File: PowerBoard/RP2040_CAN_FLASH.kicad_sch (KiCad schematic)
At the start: 52 parts, among them J1 B3B-XH-A_LF__SN_, J2 UJ31-CH-G2-SMT-TR, J4 B3B-XH-A_LF__SN_, J5 Conn_02x10_Counter_Clockwise, Q1 BSS138, Q4 BSS138, Q5 BSS138, Q6 BSS138, U1 RPI2040, U5 W25Q128JVS, U7 MCP2515-xST, U8 MCP2551-I-SN, Y1 445C25D12M00000, Y2 CX532Z-A2B3C5-70-8.0D18

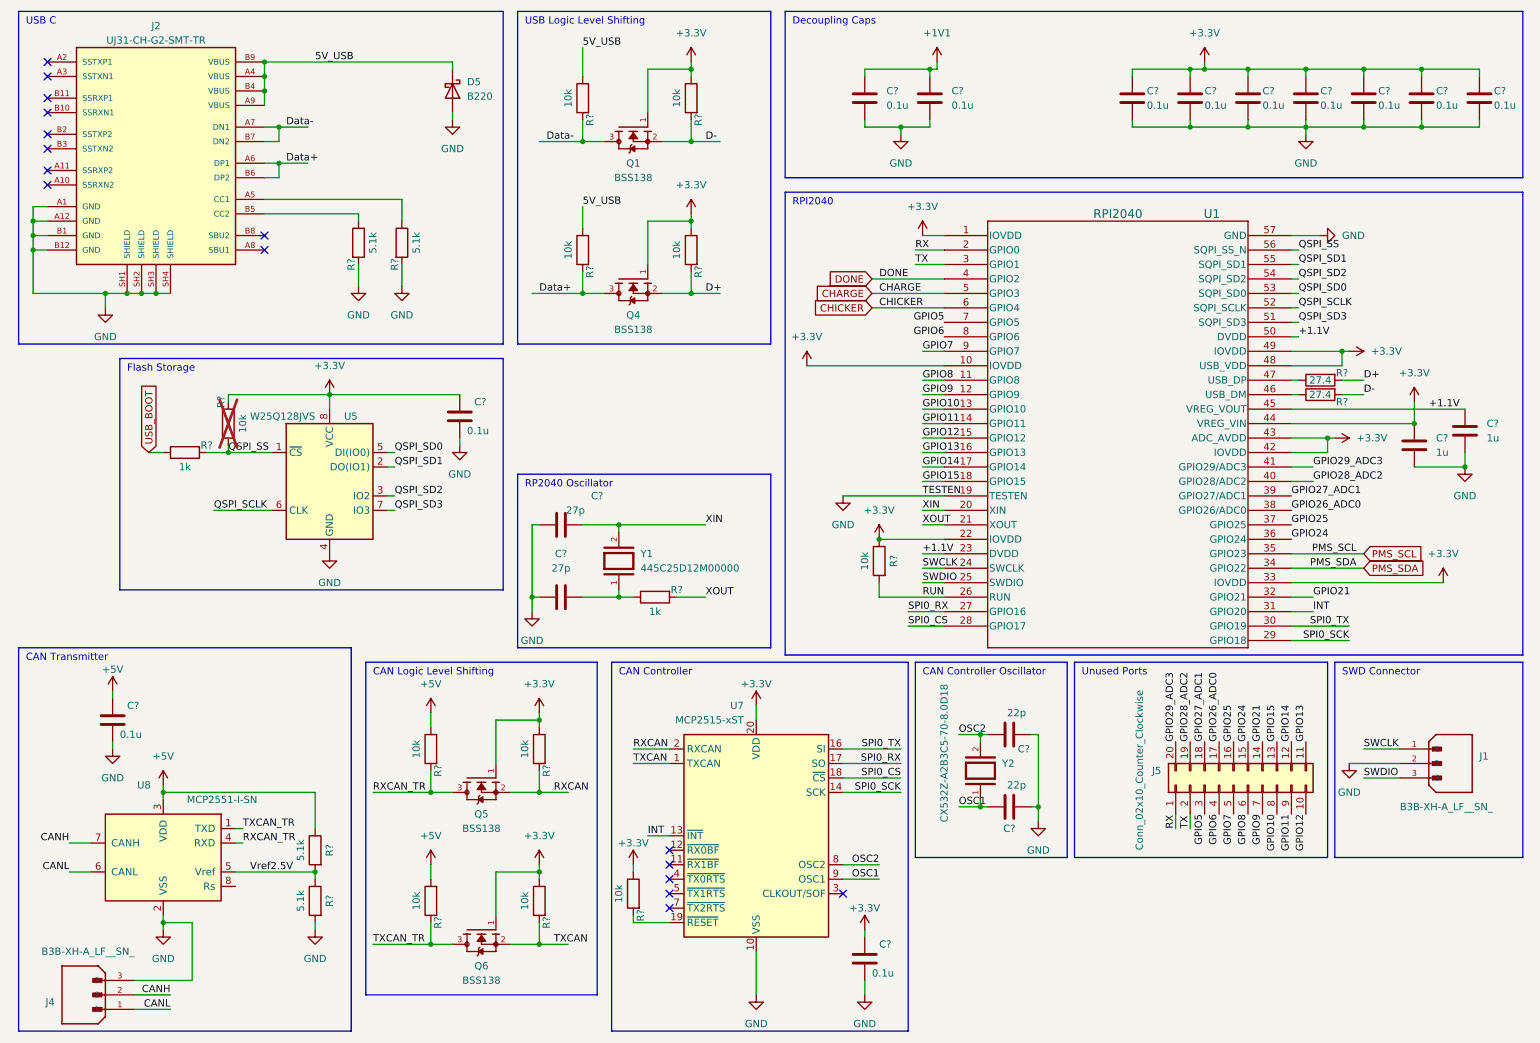
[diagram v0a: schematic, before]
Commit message: updated small details + LEDS
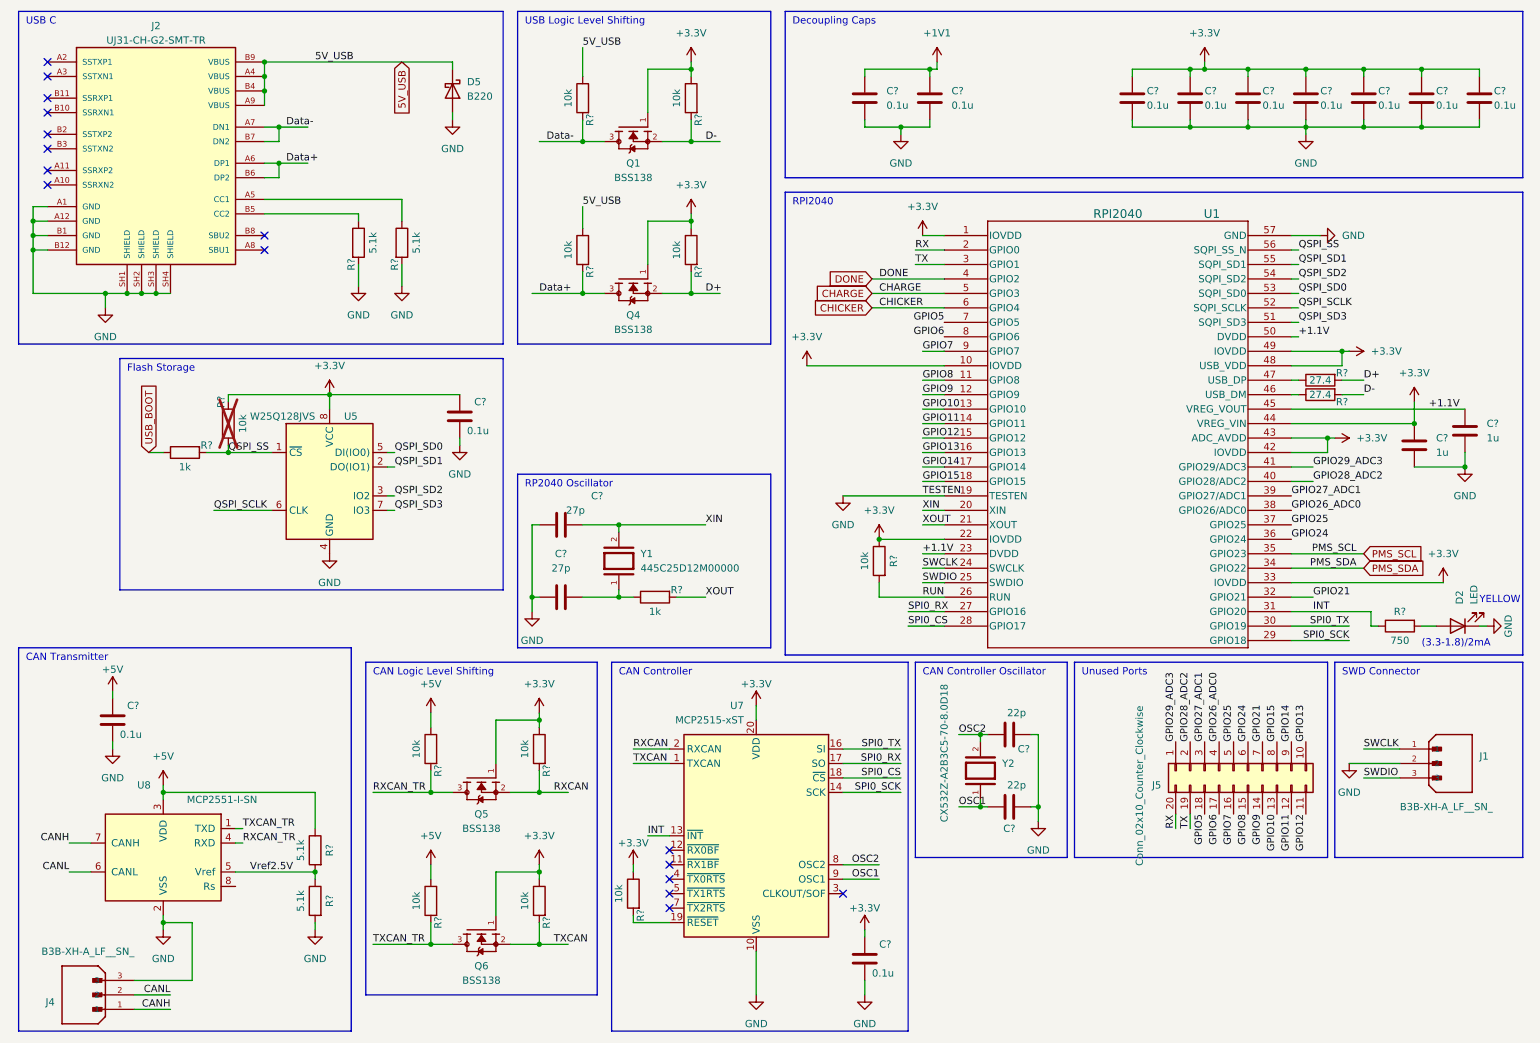
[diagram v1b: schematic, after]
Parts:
- added D2: LED, LED_SMD:LED_1206_3216Metric, symbol Device:LED
- added R?: 750, Resistor_SMD:R_0603_1608Metric, symbol Device:R
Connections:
- net CANH: now also J4.1; no longer J4.2
- net CANL: now also J4.2; no longer J4.1
- net GND: now also D2.1 (K)
- net GPIO10: now also J5.13 (Pin_13); no longer J5.8 (Pin_8)
- net GPIO11: now also J5.12 (Pin_12); no longer J5.9 (Pin_9)
- net GPIO12: now also J5.11 (Pin_11); no longer J5.10 (Pin_10)
- net GPIO13: now also J5.10 (Pin_10); no longer J5.11 (Pin_11)
- net GPIO14: now also J5.9 (Pin_9); no longer J5.12 (Pin_12)
- net GPIO15: now also J5.8 (Pin_8); no longer J5.13 (Pin_13)
- net GPIO21: now also J5.7 (Pin_7); no longer J5.14 (Pin_14)
- net GPIO24: now also J5.6 (Pin_6); no longer J5.15 (Pin_15)
- net GPIO25: now also J5.5 (Pin_5); no longer J5.16 (Pin_16)
- net GPIO26_ADC0: now also J5.4 (Pin_4); no longer J5.17 (Pin_17)
- net GPIO27_ADC1: now also J5.3 (Pin_3); no longer J5.18 (Pin_18)
- net GPIO28_ADC2: now also J5.2 (Pin_2); no longer J5.19 (Pin_19)
- net GPIO29_ADC3: now also J5.1 (Pin_1); no longer J5.20 (Pin_20)
- net GPIO5: now also J5.18 (Pin_18); no longer J5.3 (Pin_3)
- net GPIO6: now also J5.17 (Pin_17); no longer J5.4 (Pin_4)
- net GPIO7: now also J5.16 (Pin_16); no longer J5.5 (Pin_5)
- net GPIO8: now also J5.15 (Pin_15); no longer J5.6 (Pin_6)
- net GPIO9: now also J5.14 (Pin_14); no longer J5.7 (Pin_7)
- net INT: now also R?.1
- net RX: now also J5.20 (Pin_20); no longer J5.1 (Pin_1)
- net TX: now also J5.19 (Pin_19); no longer J5.2 (Pin_2)
- new net: D2.2 (A), R?.2
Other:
- note added: "(3.3-1.8)/2mA"
- note added: "YELLOW"
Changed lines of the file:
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@@
     (stroke (width 0) (type default))
   )
-  (wire (pts (xy 238.76 120.65) (xy 242.57 120.65))
+  (wire (pts (xy 238.76 120.65) (xy 252.73 120.65))
     (stroke (width 0) (type default))
   )
@@
     (stroke (width 0) (type default))
   )
-  (wire (pts (xy 220.98 156.21) (xy 220.98 158.75))
-    (stroke (width 0) (type default))
-  )
   (wire (pts (xy 40.64 152.4) (xy 40.64 151.13))
     (stroke (width 0) (type default))
@@
     (stroke (width 0) (type default))
   )
+  (wire (pts (xy 252.73 123.19) (xy 254 123.19))
+    (stroke (width 0) (type default))
+  )
   (wire (pts (xy 173.99 82.55) (xy 177.8 82.55))
     (stroke (width 0) (type default))
@@
     (stroke (width 0) (type default))
   )
+  (wire (pts (xy 218.44 156.21) (xy 218.44 158.75))
+    (stroke (width 0) (type default))
+  )
   (wire (pts (xy 261.62 35.56) (xy 251.46 35.56))
     (stroke (width 0) (type default))
@@
     (stroke (width 0) (type default))
   )
-  (wire (pts (xy 218.44 156.21) (xy 218.44 158.75))
-    (stroke (width 0) (type default))
-  )
   (wire (pts (xy 24.13 161.29) (xy 27.94 161.29))
     (stroke (width 0) (type default))
@@
     (stroke (width 0) (type default))
   )
+  (wire (pts (xy 271.78 123.19) (xy 273.05 123.19))
+    (stroke (width 0) (type default))
+  )
+  (wire (pts (xy 261.62 123.19) (xy 264.16 123.19))
+    (stroke (width 0) (type default))
+  )
   (wire (pts (xy 69.85 82.55) (xy 69.85 85.09))
     (stroke (width 0) (type default))
@@
     (stroke (width 0) (type default))
   )
+  (wire (pts (xy 252.73 123.19) (xy 252.73 120.65))
+    (stroke (width 0) (type default))
+  )
   (wire (pts (xy 58.42 41.91) (xy 60.96 41.91))
     (stroke (width 0) (type default))
@@
     (stroke (width 0) (type default))
   )
+  (wire (pts (xy 220.98 156.21) (xy 220.98 158.75))
+    (stroke (width 0) (type default))
+  )
   (wire (pts (xy 251.46 144.78) (xy 257.81 144.78))
     (stroke (width 0) (type default))
@@
     (effects (font (size 1.27 1.27)) (justify left bottom))
   )
+  (text "YELLOW" (at 271.78 119.38 0)
+    (effects (font (size 1.27 1.27) (color 251 249 0 1)) (justify left bottom))
+  )
   (text "CAN Controller\n" (at 120.65 132.08 0)
     (effects (font (size 1.27 1.27)) (justify left bottom))
@@
     (effects (font (size 1.27 1.27)) (justify left bottom))
   )
+  (text "(3.3-1.8)/2mA" (at 261.62 127 0)
+    (effects (font (size 1.27 1.27) (color 0 4 0 1)) (justify left bottom))
+  )
   (label "SPI0_CS" (at 171.45 123.19 0) (fields_autoplaced)
     (effects (font (size 1.27 1.27)) (justify left bottom))
@@
     (effects (font (size 1.27 1.27)) (justify left bottom))
   )
-  (label "CANL" (at 41.91 190.5 180) (fields_autoplaced)
-    (effects (font (size 1.27 1.27)) (justify right bottom))
-  )
   (label "GPIO26_ADC0" (at 238.76 102.87 0) (fields_autoplaced)
     (effects (font (size 1.27 1.27)) (justify left bottom))
@@
     (effects (font (size 1.27 1.27)) (justify left bottom))
   )
+  (label "CANL" (at 41.91 187.96 180) (fields_autoplaced)
+    (effects (font (size 1.27 1.27)) (justify right bottom))
+  )
   (label "XOUT" (at 135.89 118.11 0) (fields_autoplaced)
     (effects (font (size 1.27 1.27)) (justify left bottom))
@@
     (effects (font (size 1.27 1.27)) (justify left bottom))
   )
+  (label "CANH" (at 41.91 190.5 180) (fields_autoplaced)
+    (effects (font (size 1.27 1.27)) (justify right bottom))
+  )
   (label "GPIO6" (at 226.06 156.21 270) (fields_autoplaced)
     (effects (font (size 1.27 1.27)) (justify right bottom))
@@
     (effects (font (size 1.27 1.27)) (justify right bottom))
   )
-  (label "CANH" (at 41.91 187.96 180) (fields_autoplaced)
-    (effects (font (size 1.27 1.27)) (justify right bottom))
-  )
   (label "RXCAN_TR" (at 77.47 152.4 0) (fields_autoplaced)
     (effects (font (size 1.27 1.27)) (justify left bottom))
@@
     )
   )
+  (global_label "5V_USB" (shape input) (at 82.55 24.13 270) (fields_autoplaced)
+    (effects (font (size 1.27 1.27)) (justify right))
+    (property "Intersheetrefs" "${INTERSHEET_REFS}" (at 82.55 34.1909 90)
+      (effects (font (size 1.27 1.27)) (justify right) hide)
+    )
+  )
+  (symbol (lib_id "Device:R") (at 257.81 123.19 90) (mirror x) (unit 1)
+    (in_bom yes) (on_board yes) (dnp no)
+    (property "Reference" "R?" (at 257.81 120.65 90)
+      (effects (font (size 1.27 1.27)))
+    )
+    (property "Value" "750" (at 257.81 125.73 90)
+      (effects (font (size 1.27 1.27)))
+    )
+    (property "Footprint" "Resistor_SMD:R_0603_1608Metric" (at 257.81 121.412 90)
+      (effects (font (size 1.27 1.27)) hide)
+    )
+    (property "Datasheet" "~" (at 257.81 123.19 0)
+      (effects (font (size 1.27 1.27)) hide)
+    )
+    (pin "1")
+    (pin "2")
+    (instances
+      (project "POWER_BOARD"
+        (path "/1a9ce3e8-a091-496c-9c5f-e7b2eb60e275"
+          (reference "R?") (unit 1)
+        )
+        (path "/1a9ce3e8-a091-496c-9c5f-e7b2eb60e275/44109b35-87db-4b37-b749-86ba1243ffef"
+          (reference "R40") (unit 1)
+        )
+        (path "/1a9ce3e8-a091-496c-9c5f-e7b2eb60e275/aa68550e-c35d-4fef-b4e5-f1eb6225215f"
+          (reference "R53") (unit 1)
+        )
+      )
+    )
+  )
   (symbol (lib_id "Diode:B220") (at 91.44 29.21 270) (unit 1)
     (in_bom yes) (on_board yes) (dnp no) (fields_autoplaced)
@@
     )
   )
-  (symbol (lib_id "Connector_Generic:Conn_02x10_Counter_Clockwise") (at 228.6 151.13 90) (unit 1)
+  (symbol (lib_id "Connector_Generic:Conn_02x10_Counter_Clockwise") (at 228.6 148.59 90) (mirror x) (unit 1)
     (in_bom yes) (on_board yes) (dnp no)
-    (property "Reference" "J5" (at 215.9 148.59 90)
+    (property "Reference" "J5" (at 215.9 151.13 90)
       (effects (font (size 1.27 1.27)) (justify left))
     )
-    (property "Value" "Conn_02x10_Counter_Clockwise" (at 212.09 162.56 0)
+    (property "Value" "Conn_02x10_Counter_Clockwise" (at 212.09 137.16 0)
       (effects (font (size 1.27 1.27)) (justify left))
     )
-    (property "Footprint" "Connector_PinHeader_2.54mm:PinHeader_2x10_P2.54mm_Vertical" (at 228.6 151.13 0)
+    (property "Footprint" "Connector_PinHeader_2.54mm:PinHeader_2x10_P2.54mm_Vertical" (at 228.6 148.59 0)
       (effects (font (size 1.27 1.27)) hide)
     )
-    (property "Datasheet" "~" (at 228.6 151.13 0)
+    (property "Datasheet" "~" (at 228.6 148.59 0)
       (effects (font (size 1.27 1.27)) hide)
     )
@@
     )
   )
+  (symbol (lib_id "power:GND") (at 273.05 123.19 90) (unit 1)
+    (in_bom yes) (on_board yes) (dnp no)
+    (property "Reference" "#PWR07" (at 279.4 123.19 0)
+      (effects (font (size 1.27 1.27)) hide)
+    )
+    (property "Value" "GND" (at 276.86 123.19 0)
+      (effects (font (size 1.27 1.27)))
+    )
+    (property "Footprint" "" (at 273.05 123.19 0)
+      (effects (font (size 1.27 1.27)) hide)
+    )
+    (property "Datasheet" "" (at 273.05 123.19 0)
+      (effects (font (size 1.27 1.27)) hide)
+    )
+    (pin "1")
+    (instances
+      (project "POWER_BOARD"
+        (path "/1a9ce3e8-a091-496c-9c5f-e7b2eb60e275"
+          (reference "#PWR07") (unit 1)
+        )
+        (path "/1a9ce3e8-a091-496c-9c5f-e7b2eb60e275/aa68550e-c35d-4fef-b4e5-f1eb6225215f"
+          (reference "#PWR021") (unit 1)
+        )
+        (path "/1a9ce3e8-a091-496c-9c5f-e7b2eb60e275/44109b35-87db-4b37-b749-86ba1243ffef"
+          (reference "#PWR064") (unit 1)
+        )
+      )
+    )
+  )
   (symbol (lib_id "power:+5V") (at 31.75 134.62 0) (unit 1)
     (in_bom yes) (on_board yes) (dnp no)
@@
         )
       )
+    )
+  )
+  (symbol (lib_id "Device:LED") (at 267.97 123.19 180) (unit 1)
+    (in_bom yes) (on_board yes) (dnp no) (fields_autoplaced)
+    (property "Reference" "D2" (at 268.2875 119.38 90)
+      (effects (font (size 1.27 1.27)) (justify right))
+    )
+    (property "Value" "LED" (at 270.8275 119.38 90)
+      (effects (font (size 1.27 1.27)) (justify right))
+    )
+    (property "Footprint" "LED_SMD:LED_1206_3216Metric" (at 267.97 123.19 0)
+      (effects (font (size 1.27 1.27)) hide)
+    )
+    (property "Datasheet" "APT3216LSYCK/J3-PRV" (at 267.97 123.19 0)
+      (effects (font (size 1.27 1.27)) hide)
+    )
+    (pin "1")
+    (pin "2")
+    (instances
+      (project "POWER_BOARD"
+        (path "/1a9ce3e8-a091-496c-9c5f-e7b2eb60e275"
+          (reference "D2") (unit 1)
+        )
+        (path "/1a9ce3e8-a091-496c-9c5f-e7b2eb60e275/aa68550e-c35d-4fef-b4e5-f1eb6225215f"
+          (reference "D4") (unit 1)
+        )
+        (path "/1a9ce3e8-a091-496c-9c5f-e7b2eb60e275/44109b35-87db-4b37-b749-86ba1243ffef"
+          (reference "D9") (unit 1)
+        )
+      )

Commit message: update to layout
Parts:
- removed J2: UJ31-CH-G2-SMT-TR, bots:UJ31-CH-G2-SMT-TR, symbol bots:UJ31-CH-G2-SMT-TR
- removed Q5, Q6: BSS138, bots:SOT95P240X111-3N, symbol bots:BSS138
- removed R? (x4): 10k, Resistor_SMD:R_0603_1608Metric, symbol Device:R
- added J2: USB4145-03-0170-C_REVA2, bots:GCT_USB4145-03-0170-C_REVA2, symbol bots:USB4145-03-0170-C_REVA2
- C? (x18): footprint Capacitor_SMD:C_0603_1608Metric -> bots:C_0603_1608Metric
- D2: footprint LED_SMD:LED_1206_3216Metric -> bots:LED_1206_3216Metric
- D5: footprint Diode_SMD:D_SMB -> bots:D_SMB
- J5: footprint Connector_PinHeader_2.54mm:PinHeader_2x10_P2.54mm_Vertical -> bots:PinHeader_2x10_P2.54mm_Vertical
- R? (x15): footprint Resistor_SMD:R_0603_1608Metric -> bots:R_0603_1608Metric
- U7: footprint Package_SO:TSSOP-20_4.4x6.5mm_P0.65mm -> bots:TSSOP-20_4.4x6.5mm_P0.65mm
- U8: footprint Package_SO:SOIC-8_3.9x4.9mm_P1.27mm -> bots:SOIC-8_3.9x4.9mm_P1.27mm
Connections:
- net +1V1 is gone; now on net +1.1V: C?.1, C?.1
- net +5V is gone; now on net +3.3V: C?.1, R?.1, U8.3 (VDD)
- net RXCAN_TR is gone; now on net RXCAN: U8.4 (RXD)
- net TXCAN_TR is gone; now on net TXCAN: U8.1 (TXD)
- net 5V_USB: now also J2.A4 (VBUS_A), J2.A9 (VBUS_A), J2.B4 (VBUS_B), J2.B9 (VBUS_B)
- net CHARGE: now also U1.7 (GPIO5); no longer U1.5 (GPIO3)
- net CHICKER: now also U1.4 (GPIO2); no longer U1.6 (GPIO4)
- net DONE: now also U1.6 (GPIO4); no longer U1.4 (GPIO2)
- net Data+: now also J2.A6 (DP1), J2.B6 (DP2)
- net Data-: now also J2.A7 (DN1), J2.B7 (DN2)
- net GND: now also J2.A1 (GND_A), J2.A12 (GND_A), J2.B1 (GND_B), J2.B12 (GND_B), J2.S1 (SHIELD), J2.S2 (SHIELD), J2.S3 (SHIELD), J2.S4 (SHIELD)
- net DR+: now reaches R?.1, U1.47 (USB_DP)
- net DR-: now reaches R?.1, U1.46 (USB_DM)
- net CC1: now reaches R?.1
- net CC1: now also J2.A5 (CC1)
- net CC2: now reaches R?.1
- net CC2: now also J2.B5 (CC2)
- net GPIO5: no longer names the net of J5.18 (Pin_18)
- net GPIO5: no longer U1.7 (GPIO5)
- net Vref2.5V renamed Vref1.65V
- new net CHIP_EXTRA: U1.5 (GPIO3)
- no-connect marks 16 -> 8
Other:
- note removed: "CAN Logic Level Shifting"
- moved on the sheet: C?, D5, J4, R?, U7, U8, Y2
